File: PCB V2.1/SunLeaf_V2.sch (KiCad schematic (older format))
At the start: 0 parts

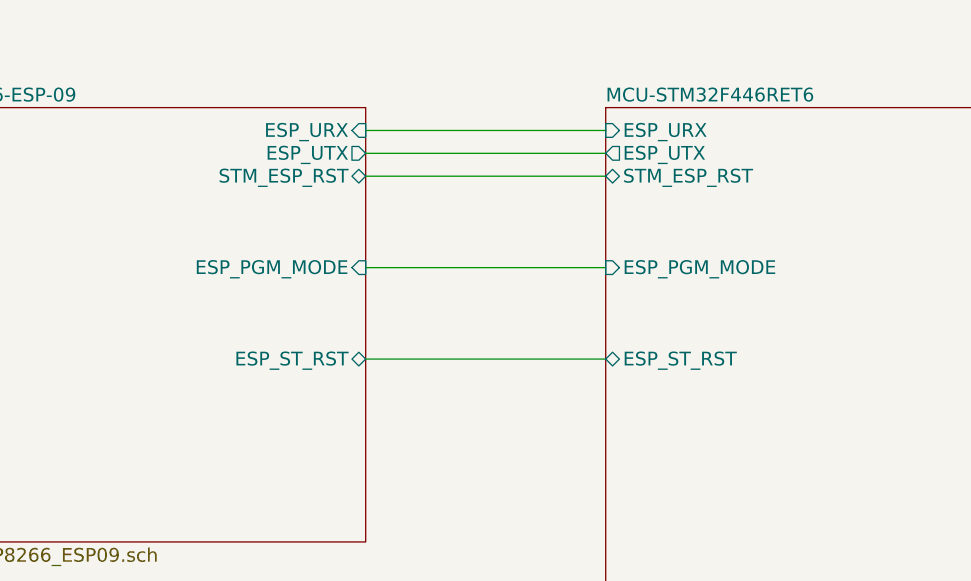
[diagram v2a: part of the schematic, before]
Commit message: OTA
This commit contains adjustments to the schematics for over the air
update/programming of STM32 via the ESP8266 using its internal
bootloader. The two processors have been wired together to suppor this
fucntions, they can toggle reset of eachother and load firmware over
UART. Still deciding what reset signal pin on the STM32 to use fo rthis
purpose, next commit.
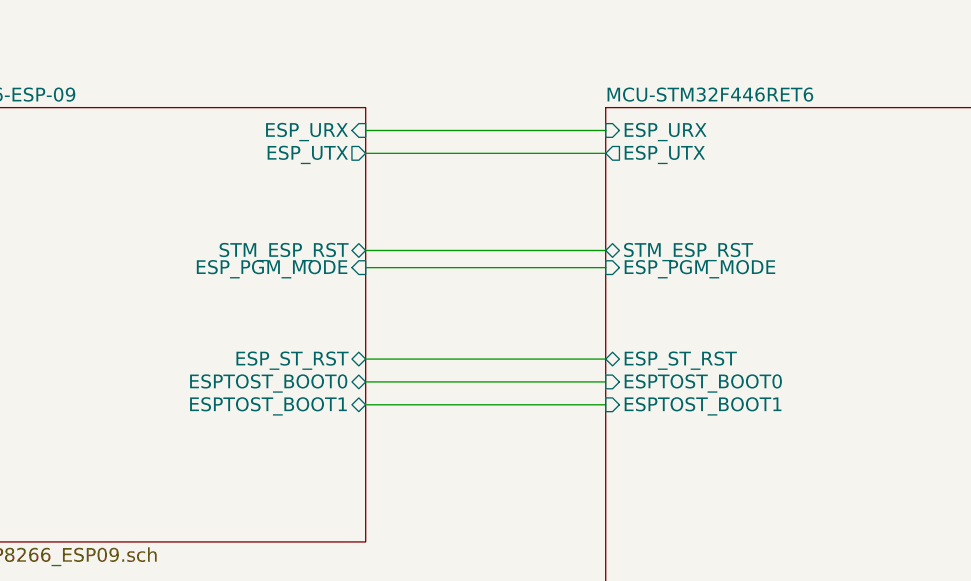
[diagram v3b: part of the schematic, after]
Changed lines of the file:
@@
 LIBS:HydroPWNics_Lib
 LIBS:ESP32-footprints-Shem-Lib
+LIBS:ESP8266
 LIBS:SunLeaf_V2-cache
 EELAYER 25 0
@@
 F12 "ANIO_0" B R 7850 5100 60
 F13 "ESP_ST_RST" B L 4050 3700 60
-F14 "STM_ESP_RST" B L 4050 2900 60
+F14 "STM_ESP_RST" B L 4050 3225 60
 F15 "ANIO_3" B R 7850 5400 60
 F16 "ANIO_2" B R 7850 5300 60
@@
 F25 "ESP_PGM_MODE" I L 4050 3300 60
 F26 "VBUS" I L 4050 5050 60
+F27 "ESPTOST_BOOT0" I L 4050 3800 60
+F28 "ESPTOST_BOOT1" I L 4050 3900 60
 $EndSheet
 $Sheet
@@
 F2 "ESP_URX" I R 3000 2700 60
 F3 "ESP_UTX" O R 3000 2800 60
-F4 "STM_ESP_RST" B R 3000 2900 60
+F4 "STM_ESP_RST" B R 3000 3225 60
 F5 "ESP_ST_RST" B R 3000 3700 60
 F6 "ESP_PGM_MODE" I R 3000 3300 60
+F7 "ESPTOST_BOOT0" B R 3000 3800 60
+F8 "ESPTOST_BOOT1" B R 3000 3900 60
 $EndSheet
 $Sheet
@@
 SunLeaf 0.2a System Overview
 Wire Wire Line
-	4050 2900 3000 2900
+	4050 3225 3000 3225
 Wire Wire Line
 	3000 2800 4050 2800
@@
 Wire Wire Line
 	9200 2800 7850 2800
+Wire Wire Line
+	3000 3900 4050 3900
+Wire Wire Line
+	4050 3800 3000 3800
 $EndSCHEMATC

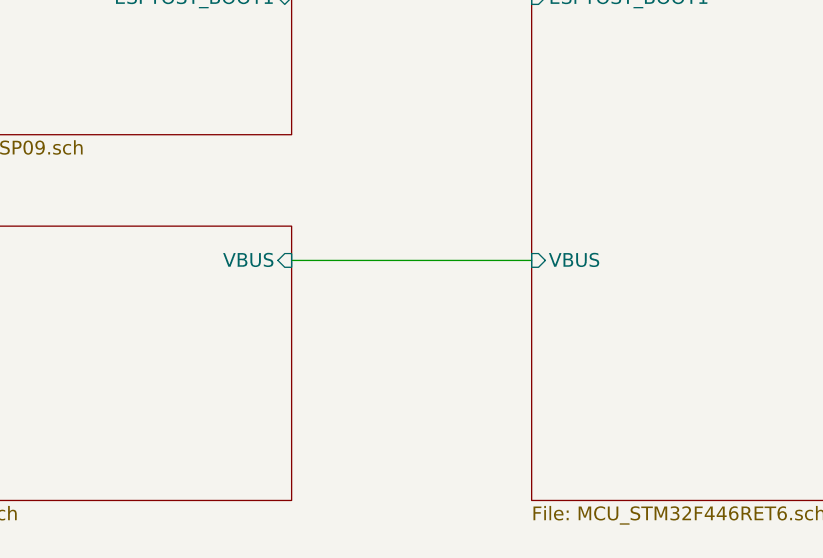
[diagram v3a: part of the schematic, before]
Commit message: Battery Monitoring & OTA
OTA signals between both processors solidified and routed. Battery
monitoring added as voltage divider into ADC channel. All but done
pending some small tweaks.
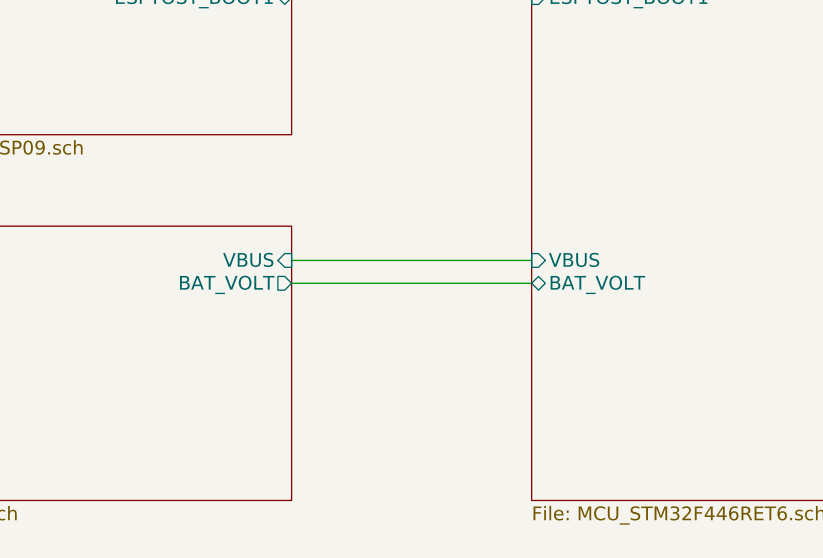
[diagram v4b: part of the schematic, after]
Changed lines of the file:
@@
 F27 "ESPTOST_BOOT0" I L 4050 3800 60
 F28 "ESPTOST_BOOT1" I L 4050 3900 60
+F29 "BAT_VOLT" B L 4050 5150 60
 $EndSheet
 $Sheet
@@
 F1 "Power_system.sch" 60
 F2 "VBUS" I R 3000 5050 60
+F3 "BAT_VOLT" O R 3000 5150 60
 $EndSheet
 $Sheet
@@
 Wire Wire Line
 	4050 3800 3000 3800
+Wire Wire Line
+	4050 5150 3000 5150
 $EndSCHEMATC
